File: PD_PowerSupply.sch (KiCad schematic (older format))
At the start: 100 parts, among them J1 Connector, J2 Connector, J3 Connector, J4 Connector, P0.13 TestPoint, P0.14 TestPoint, P0.15 TestPoint, P0.16 TestPoint, P0.17 TestPoint, P0.19 TestPoint, P0.20 TestPoint, P0.21 TestPoint, Q1 STL6P3LLH6, Q2 STL6P3LLH6, Q3 MMBT3906, Q4 MMBT3906, U1 nRF52840, U2 STUSB4500QTR, U3 STM32L432KCUx, U4 LTM8074IY#PBF, U5 LTC2972, U6 LTM8074IY#PBF, U7 LTM8074IY#PBF

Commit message: STUSB in progress
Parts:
- removed C5: .1uF, Capacitor_SMD:C_0603_1608Metric, symbol Device:C
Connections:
- wire segments 402 -> 401
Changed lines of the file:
@@
-	1    0    0    -1
-$EndComp
-$Comp
-L Device:C C5
-U 1 1 5F242A3D
-P 10100 11250
-F 0 "C5" H 10150 11350 50  0000 L CNN
-F 1 ".1uF" H 10150 11150 50  0000 L CNN
-F 2 "Capacitor_SMD:C_0603_1608Metric" H 10138 11100 50  0001 C CNN
-F 3 "~" H 10100 11250 50  0001 C CNN
-	1    10100 11250
 	1    0    0    -1
 $EndComp
@@
 Wire Wire Line
 	9500 11100 9800 11100
-Connection ~ 9800 11100
-Wire Wire Line
-	9800 11100 10100 11100
 Wire Wire Line
 	10100 11400 10100 11450
@@
 Wire Wire Line
 	9800 11400 10100 11400
-Connection ~ 10100 11400
 Wire Wire Line
 	8650 11100 8650 11550

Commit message: changed testpoints
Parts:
- removed TP3, TP4: TestPoint, TestPoint:TestPoint_Pad_D1.0mm, symbol Connector:TestPoint
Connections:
- wire segments 401 -> 397
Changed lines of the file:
@@
 	9550 12550 9250 12550
-$Comp
-L Connector:TestPoint TP3
-U 1 1 5F1F3F07
-P 8050 12300
-F 0 "TP3" H 8000 12550 50  0000 L CNN
-F 1 "TestPoint" H 8108 12327 50  0001 L CNN
-F 2 "TestPoint:TestPoint_Pad_D1.0mm" H 8250 12300 50  0001 C CNN
-F 3 "~" H 8250 12300 50  0001 C CNN
-	1    8050 12300
-	1    0    0    -1
-$EndComp
-$Comp
-L Connector:TestPoint TP4
-U 1 1 5F234221
-P 7900 12300
-F 0 "TP4" H 7850 12550 50  0000 L CNN
-F 1 "TestPoint" H 7958 12327 50  0001 L CNN
-F 2 "TestPoint:TestPoint_Pad_D1.0mm" H 8100 12300 50  0001 C CNN
-F 3 "~" H 8100 12300 50  0001 C CNN
-	1    7900 12300
-	1    0    0    -1
-$EndComp
-Wire Wire Line
-	8050 12300 8050 12350
-Wire Wire Line
-	8050 12350 8250 12350
-Wire Wire Line
-	7900 12300 7900 12450
-Wire Wire Line
-	7900 12450 8250 12450
 $Comp
 L FTSH-105-01-L-DV-K:FTSH-105-01-L-DV-K PH2

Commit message: create single channel version w LTC7106-1 SPI DAC
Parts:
- removed +3V3, GND1, P0.13, P0.14, P0.15, P0.16, P0.17, P0.19, P0.20, P0.21, PMB_SCL1, PMB_SDA1: TestPoint, TestPoint:TestPoint_Pad_D1.0mm, symbol Connector:TestPoint
- removed C14, C15: .1uF, Capacitor_SMD:C_0603_1608Metric, symbol Device:C
- removed C18: 10uF, Capacitor_SMD:C_0603_1608Metric, symbol Device:C
- removed D2: GREEN 0805, LED_SMD:LED_0805_2012Metric, symbol Device:LED
- removed D3: RED 0805, LED_SMD:LED_0805_2012Metric, symbol Device:LED
- removed D5: ORANGE 0805, LED_SMD:LED_0805_2012Metric, symbol Device:LED
- removed J2: Connector, Connector_AMASS:AMASS_XT30PW-F_1x02_P2.50mm_Horizontal, symbol Connector:Conn_01x02_Male
- removed J3, J4: Connector, Connector_PinHeader_2.54mm:PinHeader_1x02_P2.54mm_Vertical, symbol Connector:Conn_01x02_Male
- removed JP1, JP2, JP3: SolderJumper_2_Bridged, Jumper:SolderJumper-2_P1.3mm_Bridged_RoundedPad1.0x1.5mm, symbol Jumper:SolderJumper_2_Bridged
- removed PH1: FTSH-105-01-L-DV-K, SAMTEC_FTSH-105-01-L-DV-K, symbol FTSH-105-01-L-DV-K:FTSH-105-01-L-DV-K
- removed Q3, Q4: MMBT3906, Package_TO_SOT_SMD:SOT-23, symbol Transistor_BJT:MMBT3906
- removed R19, R21, R23, R24, R26, R27, R7: 10k, Resistor_SMD:R_0603_1608Metric, symbol Device:R_US
- removed R20, R28: 20m, Resistor_SMD:R_1206_3216Metric, symbol Device:R_US
- removed R22, R25, R29: R_US, Resistor_SMD:R_0603_1608Metric, symbol Device:R_US
- removed R30: 23.7k, Resistor_SMD:R_0603_1608Metric, symbol Device:R_US
- removed R31: 76.8k, Resistor_SMD:R_0603_1608Metric, symbol Device:R_US
- removed R32, R33: 40.2k, Resistor_SMD:R_0603_1608Metric, symbol Device:R_US
- removed R36: 300, Resistor_SMD:R_0603_1608Metric, symbol Device:R_US
- removed U3: STM32L432KCUx, Package_DFN_QFN:QFN-32-1EP_5x5mm_P0.5mm_EP3.45x3.45mm, symbol MCU_ST_STM32L4:STM32L432KCUx
- removed U5: LTC2972, LTC2972:LTC2972, symbol LTC2972_SCH:LTC2972
- removed U6, U7: LTM8074IY#PBF, LTM8074IY_PBF:BGA25C65P5X5_400X400X198N, symbol LTM8074IY_PBF:LTM8074IY#PBF
- added C21: 820pF, Capacitor_SMD:C_0603_1608Metric, symbol Device:C
- added C22: 1uF, Capacitor_SMD:C_0603_1608Metric, symbol Device:C
- added C23: 4.7uF, Capacitor_SMD:C_0603_1608Metric, symbol Device:C
- added C5: .1uF, Capacitor_SMD:C_0603_1608Metric, symbol Device:C
- added D2: WS2812B, LED_SMD:LED_WS2812B_PLCC4_5.0x5.0mm_P3.2mm, symbol LED:WS2812B
- added D3, D5: D_Schottky, Diode_SMD:D_0603_1608Metric_Castellated, symbol Device:D_Schottky
- added J2: Screw Terminal, TerminalBlock_Phoenix:TerminalBlock_Phoenix_MKDS-1,5-2_1x02_P5.00mm_Horizontal, symbol Connector:Screw_Terminal_01x02
- added R?: 10k, Resistor_SMD:R_0603_1608Metric, symbol Device:R_US
- added U5: AD8417, Package_SO:SOIC-8_3.9x4.9mm_P1.27mm, symbol Amplifier_Current:AD8417
- added U?: LMR16006YQ5, Package_TO_SOT_SMD:SOT-23-6, symbol Regulator_Switching:LMR16006YQ5
- added U?: LTC7106EDDB-1, DFN10_DDB, symbol 2020-04-18_18-56-16:LTC7106EDDB-1
- added X1: ABM3-32.000MHZ-D2Y-T, ABM3-32:XTAL500X320X130N, symbol ABM3-32.000MHZ-D2Y-T:ABM3-32.000MHZ-D2Y-T
- C10: value .01uF -> C
- C11: value .1uF -> 1uF
- C12: value .1uF -> 10uF
- C16: value 1uF -> 12pF
- C17: value 10nF -> 12pF
- C19: value 10uF -> .1uF; footprint Capacitor_SMD:C_0805_2012Metric -> Capacitor_SMD:C_0603_1608Metric
- C20: value 10uF -> .1nF; footprint Capacitor_SMD:C_0805_2012Metric -> Capacitor_SMD:C_0603_1608Metric
- C6: value 10nF -> .1uF
- J1: value Connector -> 2.54mm Header; footprint Connector_AMASS:AMASS_XT30PW-F_1x02_P2.50mm_Horizontal -> Connector_PinHeader_2.54mm:PinHeader_1x02_P2.54mm_Horizontal
- PH2: footprint SAMTEC_FTSH-105-01-L-DV-K -> FTSH-105-01-L-DV-K:SAMTEC_FTSH-105-01-L-DV-K
- R1: value 100k -> 20
- R10, R6: value 47.5k -> 10k
- R11: value 47.5k -> 40.2k
- R12: value 47.5k -> FEEDBACK
- R14: value 300 -> 20m; footprint Resistor_SMD:R_0603_1608Metric -> Resistor_SMD:R_1206_3216Metric
- R15: value 300 -> 10K
- R17: value R_US -> 2K
- R18: value 20m -> 10k; footprint Resistor_SMD:R_1206_3216Metric -> Resistor_SMD:R_0603_1608Metric; PN PF1206FRF070R02L -> (none)
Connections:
- net labels added: +5V, STUSB_POK2, STUSB_POK3
- net labels removed: CONTROL0, CONTROL1, FAULTB0, FAULTB1, I2C_SCL_SMBUS, I2C_SDA_SMBUS, SMBUS_ALERT, SPI_MISO, SPI_MOSI, SPI_SCK, SPI_SS, STM32_NRST, STM32_SWDCLK, STM32_SWDIO, STM32_SWO, STUSB_ALERT, UART_RX, UART_TX, VBUS
- wire segments 397 -> 287
- no-connect marks 5 -> 14
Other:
- note added: "0603"
- note added: "1206 SHUNT\n80mW @ 2A"
- note added: "32MHz"
- note added: "60V/V gain. \n2.4V @ 2A\nInternal EMI Filters"
- note added: "ADD FILTER"
- note added: "Complete NRF52 periph setup\n"
- note added: "Ground VSS_PA near antenna!"
- note added: "High current flow ->"
- note added: "LED Power\n"
- note added: "MCU Power\n"
- note added: "NRF52 Bluetooth stack will effectively limit\nADC sample rate using interrupts to < 1khz.\nRate can be increased to 50khz w/ DMA."
- note added: "Nordic Configuration 3"
- note added: "RGB LED\n"
- note added: "VBus needs 5v?\n"
- note added: "Vout/6"
- note removed: "0805\n"
- moved on the sheet: C1, C4, C7, C8, C9, D1, D4, I2C_SCL1, I2C_SDA1, PH2, Q1, Q2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

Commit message: Setup LMP92064
Wanted to avoid using the internal ADC in the nrf52
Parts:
- removed D3, D5: D_Schottky, Diode_SMD:D_0603_1608Metric_Castellated, symbol Device:D_Schottky
- removed U5: AD8417, Package_SO:SOIC-8_3.9x4.9mm_P1.27mm, symbol Amplifier_Current:AD8417
- added C?: .1uF, Capacitor_SMD:C_0603_1608Metric, symbol Device:C
- added R19: div2, Resistor_SMD:R_0603_1608Metric, symbol Device:R_US
- added U6: LMP92064SDE_NOPB, footprints:LMP92064SDE&slash_NOPB, symbol 2020-05-08_21-34-57:LMP92064SDE_NOPB
- added U?: LM1117, Package_TO_SOT_SMD:SOT-223-3_TabPin2, symbol Regulator_Linear:AMS1117
- C13: value .1uF -> 1uF
- R14: value 20m -> 30m
- R15: value 10K -> 10k
- R17: value 2K -> div1
- U5: renamed from U?; footprint DFN10_DDB -> ul_LTC7106EDDB:LTC7106EDDB
- gave numbers to parts that had none: 2
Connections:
- wire segments 287 -> 306
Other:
- note added: "1206 SHUNT\n120mW @ 2A\n\n60mV @ 2A\n(75mV max vdif)"
- note added: "INVP has 2V max\n6.5X divider\nDivider: 12V = 1.85V"
- note removed: "0603"
- note removed: "1206 SHUNT\n80mW @ 2A"
- note removed: "60V/V gain. \n2.4V @ 2A\nInternal EMI Filters"
- note removed: "ADD FILTER"
- note removed: "Ground VSS_PA near antenna!"
- note removed: "NRF52 Bluetooth stack will effectively limit\nADC sample rate using interrupts to < 1khz.\nRate can be increased to 50khz w/ DMA."
- note removed: "Vout/6"
- moved on the sheet: R14

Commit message: Correct reference ground connection
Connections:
- net GND: now also C13.2, U6.2 (REFG)
- net VOUT: now reaches C12.1, J1.2 (Pin_2), J2.1 (Pin_1), R17.1, U4.E1 (VOUT), U4.E2 (VOUT)
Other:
- note added: "1206 SHUNT\n120mW @ 2A\n\n60mV @ 2A\n(75mV max vdif)\n\n-3db @ 70khz"
- note added: "Supply may need to be 5v"
- note removed: "1206 SHUNT\n120mW @ 2A\n\n60mV @ 2A\n(75mV max vdif)"

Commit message: Added BMD-340 standalone NRF52840
Low voltage mode + usb support
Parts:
- removed C16, C17: 12pF, Capacitor_SMD:C_0603_1608Metric, symbol Device:C
- removed C19: .1uF, Capacitor_SMD:C_0603_1608Metric, symbol Device:C
- removed C20: .1nF, Capacitor_SMD:C_0603_1608Metric, symbol Device:C
- removed C21: 820pF, Capacitor_SMD:C_0603_1608Metric, symbol Device:C
- removed C22: 1uF, Capacitor_SMD:C_0603_1608Metric, symbol Device:C
- removed C23: 4.7uF, Capacitor_SMD:C_0603_1608Metric, symbol Device:C
- removed R34: 10k, Resistor_SMD:R_0603_1608Metric, symbol Device:R_US
- removed U1: nRF52840, Package_DFN_QFN:Nordic_AQFN-73-1EP_7x7mm_P0.5mm, symbol MCU_Nordic:nRF52840
- removed X1: ABM3-32.000MHZ-D2Y-T, ABM3-32:XTAL500X320X130N, symbol ABM3-32.000MHZ-D2Y-T:ABM3-32.000MHZ-D2Y-T
- added U8: BMD-340-A-R, RIGADO_BMD-340-A-R, symbol BMD-340-A-R:BMD-340-A-R
- C5: value .1uF -> 4.7uF
- PH2: FriendlyName (none) -> Cortex Debug
- gave numbers to parts that had none: 2
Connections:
- net +3V3: now also U8.17 (VCC1), U8.65 (VCCH1)
- net +5V: now also U8.66 (VBUS)
- net GND: now also U8.1 (GND), U8.16 (GND), U8.18 (GND), U8.2 (GND), U8.29 (GND), U8.3 (GND), U8.30 (GND), U8.4 (GND), U8.45 (GND), U8.46 (GND), U8.47 (GND), U8.5 (GND), U8.55 (GND)
- net I2C_SCL: now also U8.25 (P0.09)
- net I2C_SDA: now also U8.26 (P0.10)
- net STUSB_POK2: now also U8.28 (P0.12)
- net STUSB_POK3: now also U8.31 (P0.13)
- net STUSB_RESET: now also U8.27 (P0.11)
- net at D4.2 (A): now also U8.24 (P0.08)
- net MOSI: now reaches U5.1 (SDI), U6.12 (SDI)
- net MOSI: now also U8.22 (P0.06)
- net LTC7106_CSB: now reaches U5.10 (CSB)
- net LTC7106_CSB: now also U8.19 (P0.03)
- net SCLK: now reaches U5.2 (SCLK), U6.13 (SCLK)
- net SCLK: now also U8.21 (P0.05)
- net LTC7106_EN: now reaches R15.1, U5.7 (EN)
- net LTC7106_EN: now also U8.15 (P0.02)
- net MISO: now reaches R7.2, U5.9 (SDO), U6.11 (SDO)
- net MISO: now also U8.20 (P0.04)
- net LMP92064_CSB: now reaches U6.14 (CSB)
- net LMP92064_CSB: now also U8.23 (P0.07)
- net at R1.2: now also U8.36 (P0.21)
- net NRF_NRST: no longer names the net of PH2.10 (nRST)
- net NRF_NRST: now also U8.39 (P0.18/NRESET)
- net NRF_SWDCLK: no longer names the net of PH2.4 (SWDCLK)
- net NRF_SWDCLK: now also U8.43 (SWCLK)
- net NRF_SWDIO: no longer names the net of PH2.2 (SWDIO)
- net NRF_SWDIO: now also U8.44 (SWDIO)
- net NRF_SWO: no longer names the net of PH2.6 (SWO)
- net NRF_SWO: now also U8.56 (P1.00/SWO)
- net USB_DN: no longer names the net of USB1.A7 (DN1), USB1.B7 (DN2)
- net USB_DN: now also U8.67 (USB_D-)
- net USB_DP: no longer names the net of USB1.A6 (DP1), USB1.B6 (DP2)
- net USB_DP: now also U8.68 (USB_D+)
- no-connect marks 14 -> 11
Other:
- note added: "NRESET has internal pull up\nwhen programmed as NRESET"
- note added: "NRF52 is configured for low voltage mode. \n5v VBus enables USB"
- note added: "Route to resistor!"
- note removed: "32MHz"
- note removed: "LED Power\n"
- note removed: "MCU Power\n"
- note removed: "Nordic Configuration 3"
- note removed: "RGB LED\n"
- note removed: "for USB CDC\n"
- moved on the sheet: C2, C3, C5, C6, D2, D4, PH2, R1, R18, R35, R6

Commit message: add power rails, photorelay, bulk caps
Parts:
- removed C12: 10uF, Capacitor_SMD:C_0603_1608Metric, symbol Device:C
- removed U7: LM1117, Package_TO_SOT_SMD:SOT-223-3_TabPin2, symbol Regulator_Linear:AMS1117
- added C15, C17, C18: 10uF, Capacitor_SMD:C_1206_3216Metric, symbol Device:C
- added C16: .1uF, Capacitor_SMD:C_1206_3216Metric, symbol Device:C
- added C19, C20, C21, C22, C23, C24, C25, C26: 10uF, symbol Device:C
- added D3: SD1206T040S2R0, Diode_SMD:D_1206_3216Metric_Castellated, symbol Device:D_Schottky
- added L1: LQH66SN220M03L, LQH66SN220M03L:IND_LQH66SN220M03L, symbol LQH66SN220M03L:LQH66SN220M03L
- added R20: 100K, Resistor_SMD:R_0603_1608Metric, symbol Device:R_US
- added R21: 54.9K, Resistor_SMD:R_0603_1608Metric, symbol Device:R_US
- added R22: 10K, Resistor_SMD:R_0603_1608Metric, symbol Device:R_US
- added R23: 1.1K, Resistor_SMD:R_0603_1608Metric, symbol Device:R_US
- added U1: LM1117LD-3.3, Package_TO_SOT_SMD:SOT-223-3_TabPin2, symbol Regulator_Linear:AP1117-33
- added U7: TLP3542, Package_DIP:DIP-5-6_W7.62mm, symbol Relay_SolidState:TLP3542
- C10: value C -> 0.1uF
- U8: footprint RIGADO_BMD-340-A-R -> BMD-340-A-R:RIGADO_BMD-340-A-R
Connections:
- net +3V3: now also C18.1, U1.2 (VO); no longer C6.1, D2.1 (VDD)
- net +5V: now also C6.1, D2.1 (VDD), C17.1, L1.2, R21.1, U1.3 (VI)
- net GND: now also U3.2 (GND), C15.1, C17.2, C18.2, C19.2, C20.2, C21.2, C22.2, C23.2, C24.2, C25.2, C26.2, D3.2 (A), R22.2, R23.2, U1.1 (GND)
- net VOUT: now also U7.4; no longer U4.E1 (VOUT), U4.E2 (VOUT)
- net VUSB_RAW: now also U3.5 (VIN), C15.2, R20.1
- net at U3.1 (CB): now also C16.1
- net at U3.3 (FB): now also R21.2, R22.1
- net at U3.4 (~SHDN): now also R20.2
- net at U3.6 (SW): now also C16.2, D3.1 (K), L1.1
- net OUTPUT_EN: now reaches U8.32 (P0.14)
- net OUTPUT_EN: now also U7.1
- new net: R23.1, U7.2
- new net VOUT_PRE_SWITCH: C19.1, C20.1, C21.1, C22.1, C23.1, C24.1, C25.1, C26.1, U4.E1 (VOUT), U4.E2 (VOUT), U7.6
- no-connect marks 11 -> 12
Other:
- note added: "8x 1206"
- note added: "I2C1"
- note added: "Photorelay"
- note added: "Piggyback swithing regulator controller"
- note added: "Route direct to resistor!"
- note added: "SPI0"
- note removed: "Complete NRF52 periph setup\n"
- note removed: "Route to resistor!"
- note removed: "VBus needs 5v?\n"
- moved on the sheet: C6, D2, U3

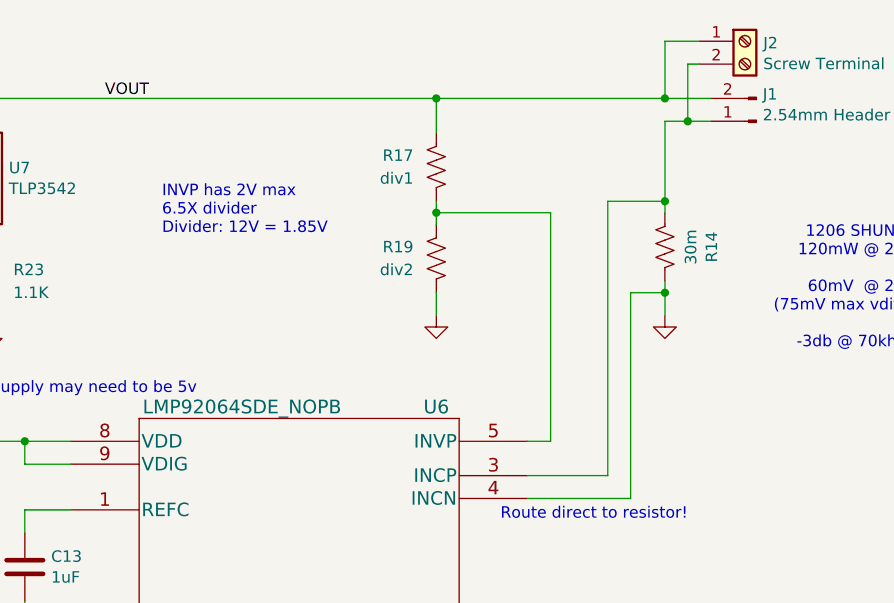
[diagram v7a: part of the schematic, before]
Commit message: Filled voltage divider values
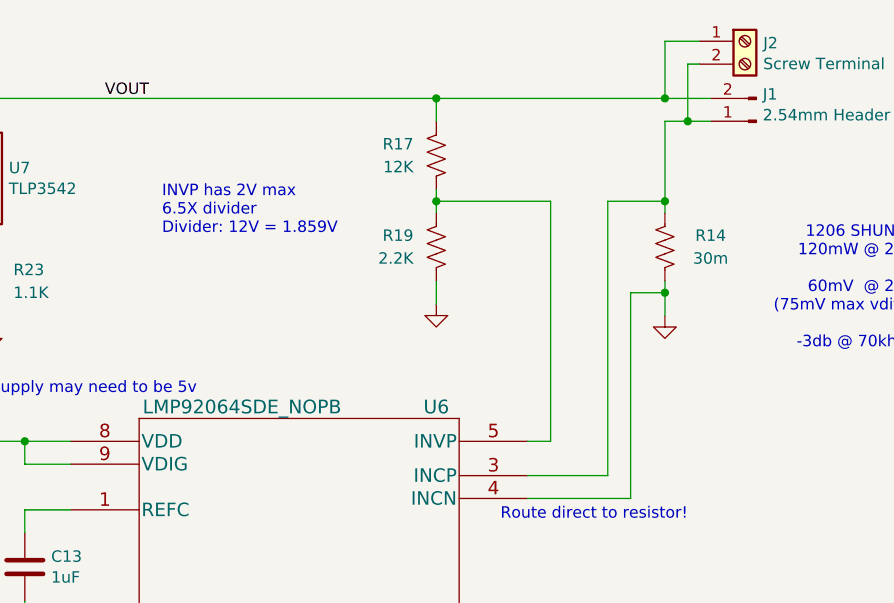
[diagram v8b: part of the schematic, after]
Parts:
- R17: value div1 -> 12K
- R19: value div2 -> 2.2K
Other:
- note added: "INVP has 2V max\n6.5X divider\nDivider: 12V = 1.859V"
- note removed: "INVP has 2V max\n6.5X divider\nDivider: 12V = 1.85V"
- moved on the sheet: R17, R19
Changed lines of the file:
@@
 U 1 1 5EB26065
 P 20150 2150
-F 0 "R14" V 19945 2150 50  0000 C CNN
-F 1 "30m" V 20036 2150 50  0000 C CNN
+F 0 "R14" H 19950 2200 50  0000 C CNN
+F 1 "30m" H 19950 2100 50  0000 C CNN
 F 2 "Resistor_SMD:R_1206_3216Metric" V 20190 2140 50  0001 C CNN
 F 3 "~" H 20150 2150 50  0001 C CNN
@@
 Wire Wire Line
 	17550 4400 17300 4400
-Wire Wire Line
-	17300 4400 17300 5450
-Wire Wire Line
-	17300 5450 10300 5450
-Wire Wire Line
-	10300 5450 10300 7250
-Wire Wire Line
-	10300 7250 4850 7250
 $Comp
 L power:+3.3V #PWR0102
@@
 1206 SHUNT\n120mW @ 2A\n\n60mV  @ 2A\n(75mV max vdif)\n\n-3db @ 70khz
 Text Notes 17950 2100 0    50   ~ 0
-INVP has 2V max\n6.5X divider\nDivider: 12V = 1.85V
+INVP has 2V max\n6.5X divider\nDivider: 12V = 1.859V
 Wire Wire Line
 	17000 3700 17000 3850
@@
 L power:GND #PWR012
 U 1 1 5ECD21A0
-P 19150 2450
-F 0 "#PWR012" H 19150 2200 50  0001 C CNN
-F 1 "GND" H 19155 2277 50  0001 C CNN
-F 2 "" H 19150 2450 50  0001 C CNN
-F 3 "" H 19150 2450 50  0001 C CNN
-	1    19150 2450
-	1    0    0    -1
-$EndComp
-Wire Wire Line
-	19150 2350 19150 2450
-Wire Wire Line
-	19150 1650 19150 1500
+P 19150 2400
+F 0 "#PWR012" H 19150 2150 50  0001 C CNN
+F 1 "GND" H 19155 2227 50  0001 C CNN
+F 2 "" H 19150 2400 50  0001 C CNN
+F 3 "" H 19150 2400 50  0001 C CNN
+	1    19150 2400
+	1    0    0    -1
+$EndComp
+Wire Wire Line
+	19150 2300 19150 2400
 $Comp
 L Device:R_US R19
 U 1 1 5EC98A3B
-P 19150 2200
-F 0 "R19" H 19250 2250 50  0000 L CNN
-F 1 "div2" H 19250 2150 50  0000 L CNN
-F 2 "Resistor_SMD:R_0603_1608Metric" V 19190 2190 50  0001 C CNN
-F 3 "~" H 19150 2200 50  0001 C CNN
-	1    19150 2200
+P 19150 2150
+F 0 "R19" H 19250 2200 50  0000 L CNN
+F 1 "2.2K" H 19250 2100 50  0000 L CNN
+F 2 "Resistor_SMD:R_0603_1608Metric" V 19190 2140 50  0001 C CNN
+F 3 "~" H 19150 2150 50  0001 C CNN
+	1    19150 2150
 	-1   0    0    -1
 $EndComp
@@
 L Device:R_US R17
 U 1 1 5EC98247
-P 19150 1800
-F 0 "R17" H 19250 1850 50  0000 L CNN
-F 1 "div1" H 19250 1750 50  0000 L CNN
-F 2 "Resistor_SMD:R_0603_1608Metric" V 19190 1790 50  0001 C CNN
-F 3 "~" H 19150 1800 50  0001 C CNN
-	1    19150 1800
+P 19150 1750
+F 0 "R17" H 19250 1800 50  0000 L CNN
+F 1 "12K" H 19250 1700 50  0000 L CNN
+F 2 "Resistor_SMD:R_0603_1608Metric" V 19190 1740 50  0001 C CNN
+F 3 "~" H 19150 1750 50  0001 C CNN
+	1    19150 1750
 	-1   0    0    -1
 $EndComp
-Wire Wire Line
-	19150 2050 19150 2000
-Wire Wire Line
-	19150 1950 19150 2000
-Connection ~ 19150 2000
-Wire Wire Line
-	19650 2000 19150 2000
-Wire Wire Line
-	19650 3000 19650 2000
 Text Label 15750 1500 0    50   ~ 0
 VOUT_PRE_SWITCH
@@
 NoConn ~ 6500 8900
 Wire Wire Line
-	19150 1500 20150 1500
-Wire Wire Line
 	5350 8900 5900 8900
 Text Label 4950 8700 0    50   ~ 0
@@
 Wire Wire Line
 	15400 1500 17000 1500
-Wire Wire Line
-	17200 1500 19150 1500
-Connection ~ 19150 1500
 $Comp
 L Device:R_US R23
@@
 	1    0    0    -1
 $EndComp
+Wire Wire Line
+	17200 1500 19150 1500
+Wire Wire Line
+	19150 1600 19150 1500
+Connection ~ 19150 1500
+Wire Wire Line
+	19150 1500 20150 1500
+Wire Wire Line
+	19150 1900 19150 1950
+Wire Wire Line
+	19650 1950 19150 1950
+Connection ~ 19150 1950
+Wire Wire Line
+	19150 1950 19150 2000
+Wire Wire Line
+	19650 1950 19650 3000
+Wire Wire Line
+	17300 4400 17300 5450
+Wire Wire Line
+	10300 7250 4850 7250
+Wire Wire Line
+	17300 5450 10300 5450
+Wire Wire Line
+	10300 5450 10300 7250
 $EndSCHEMATC
